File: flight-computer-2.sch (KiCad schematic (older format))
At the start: 69 parts, among them J1 USB4105-GF-A, J2 THR, J3 SER1, J4 SER2, J5 SER3, J6 SER4, J7 Breakout, SW1 RESET, SW2 BOOT, U1 AP2114H-3.3TRG1, U2 MUN5214DW1T1G, U3 BNO085, U4 CP2102N, U5 MPL3115A2, Y1 32.768kHz

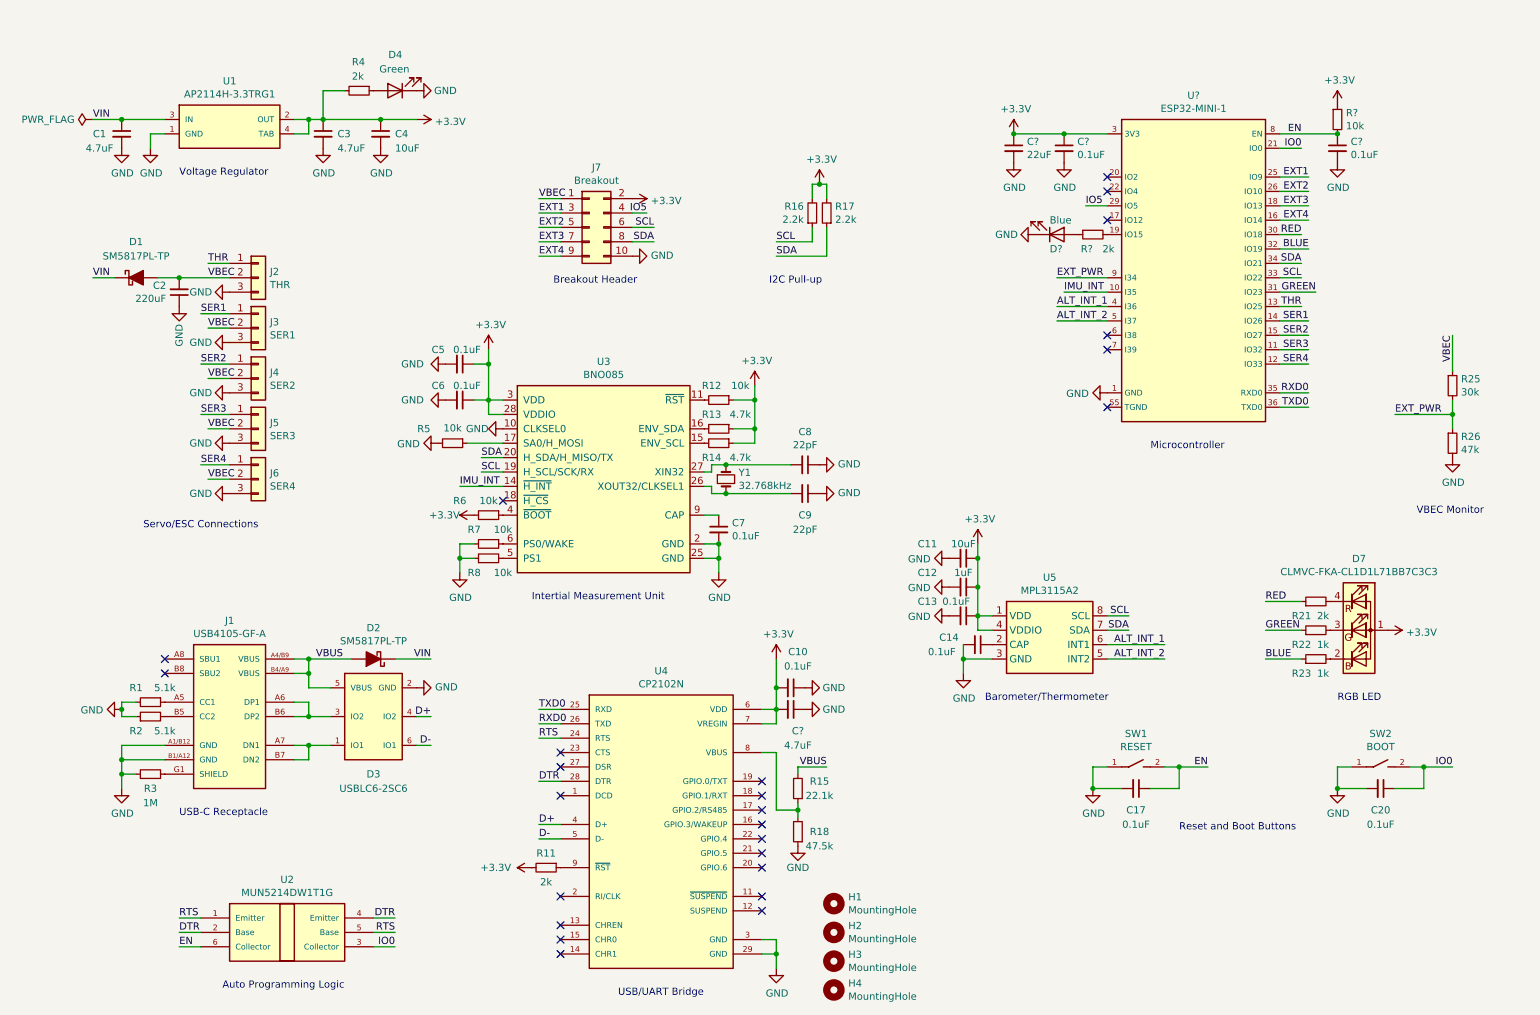
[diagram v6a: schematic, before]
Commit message: DCDC regulator and reverse current MOSFET
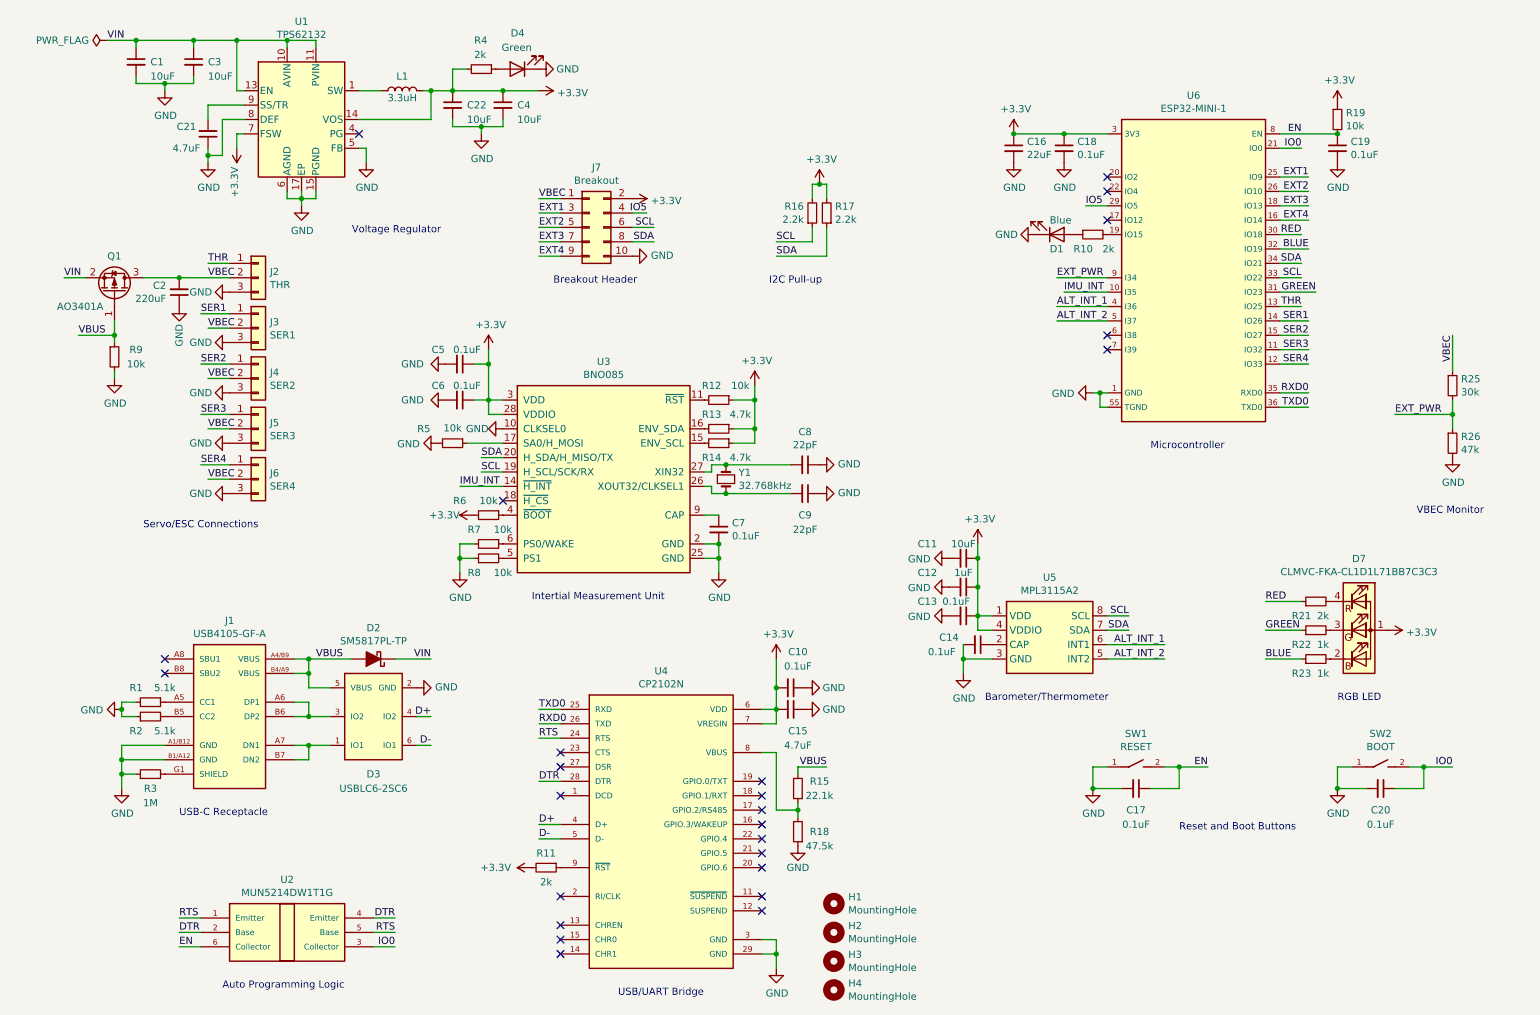
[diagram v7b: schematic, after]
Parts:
- removed D1: SM5817PL-TP, flight-computer-2:D_SOD-123F, symbol Device:D_Schottky_ALT
- removed U1: AP2114H-3.3TRG1, flight-computer-2:SOT-223, symbol flight-computer-2:AP2114H-3.3TRG1
- added C21: 4.7uF, Capacitor_SMD:C_0603_1608Metric, symbol Device:C_Small
- added C22: 10uF, Capacitor_SMD:C_0805_2012Metric, symbol Device:C_Small
- added L1: 3.3uH, flight-computer-2:L_Sunlord_MWSA0402S, symbol Device:L
- added Q1: AO3401A, Package_TO_SOT_SMD:SOT-23, symbol Transistor_FET:AO3401A
- added R9: 10k, Resistor_SMD:R_0603_1608Metric, symbol Device:R_Small
- added U1: TPS62132, Package_DFN_QFN:VQFN-16-1EP_3x3mm_P0.5mm_EP1.68x1.68mm_ThermalVias, symbol Regulator_Switching:TPS62132
- C1, C3: value 4.7uF -> 10uF; footprint Capacitor_SMD:C_0603_1608Metric -> Capacitor_SMD:C_0805_2012Metric; MPN CL10A475KP8NNNC -> GRM188R61A106KE69D
- C4: footprint Capacitor_SMD:C_0603_1608Metric -> Capacitor_SMD:C_0805_2012Metric
- U6: renamed from U?; footprint (none) -> flight-computer-2:ESP32-MINI-1
- gave numbers to parts that had none: 7
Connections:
- net +3V3: now also C22.1, L1.2, U1.14 (VOS), U1.7 (FSW); no longer C3.1
- net GND: now also U6.55 (TGND), C21.1, C22.2, R9.2, U1.15 (PGND), U1.16 (PGND), U1.17 (EP), U1.5 (FB), U1.6 (AGND), U1.8 (DEF)
- net VBEC: now also Q1.3 (D)
- net VBUS: now also Q1.1 (G), R9.1
- net VIN: now also C3.1, Q1.2 (S), U1.10 (AVIN), U1.11 (PVIN), U1.12 (PVIN), U1.13 (EN)
- new net: L1.1, U1.1 (SW), U1.2 (SW), U1.3 (SW)
- new net: C21.2, U1.9 (SS/TR)
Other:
- moved on the sheet: C4, D4, R4

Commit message: Updated annotations and parts
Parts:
- L1: MPN (none) -> 0420CDMCCDS-3R3MC
- Q1: value AO3401A -> IRLML9301; MPN (none) -> IRLML9301
- renumbered C15 to C11, C8 to C12, C9 to C13, C11 to C14, C12 to C15, C13 to C16, C14 to C17, C16 to C18, C18 to C19, C17 to C20, C19 to C21, C20 to C22, C21 to C4, C22 to C5, C5 to C6, C6 to C7, C4 to C8, C7 to C9, D2 to D1, D3 to D2, D4 to D3, D1 to D4, D7 to D5, R9 to R1, R11 to R10, R12 to R11, R13 to R12, R14 to R13, R15 to R14, R18 to R15, R10 to R18, R21 to R19, R1 to R2, R22 to R20, R23 to R21, R19 to R22, R25 to R23, R26 to R24, R2 to R3, R3 to R4, R4 to R6, R6 to R7, R7 to R8, R8 to R9, U2 to U1, U1 to U2
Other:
- moved on the sheet: R1
